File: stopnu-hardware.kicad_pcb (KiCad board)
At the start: 4 copper layers, 94 x 131 mm, 66 parts, among them CN1 SM04B-SRSS-TB (LF)(SN), CN2 OQ0232510000G, CN3 OQ0232510000G, CN4 OQ0232510000G, CN5 OQ0232510000G, CN6 OQ0432510000G, J1 Conn_02x15_Odd_Even, U1 WIFI_KIT_32__V3_, U19 SY6280AAC, U2 74HCT1G125GW-Q100H, U3 LD1117V33, U4 74HCT1G125GW-Q100H, U5 LTV-817S, U6 LTV-817S, U7 LTV-817S

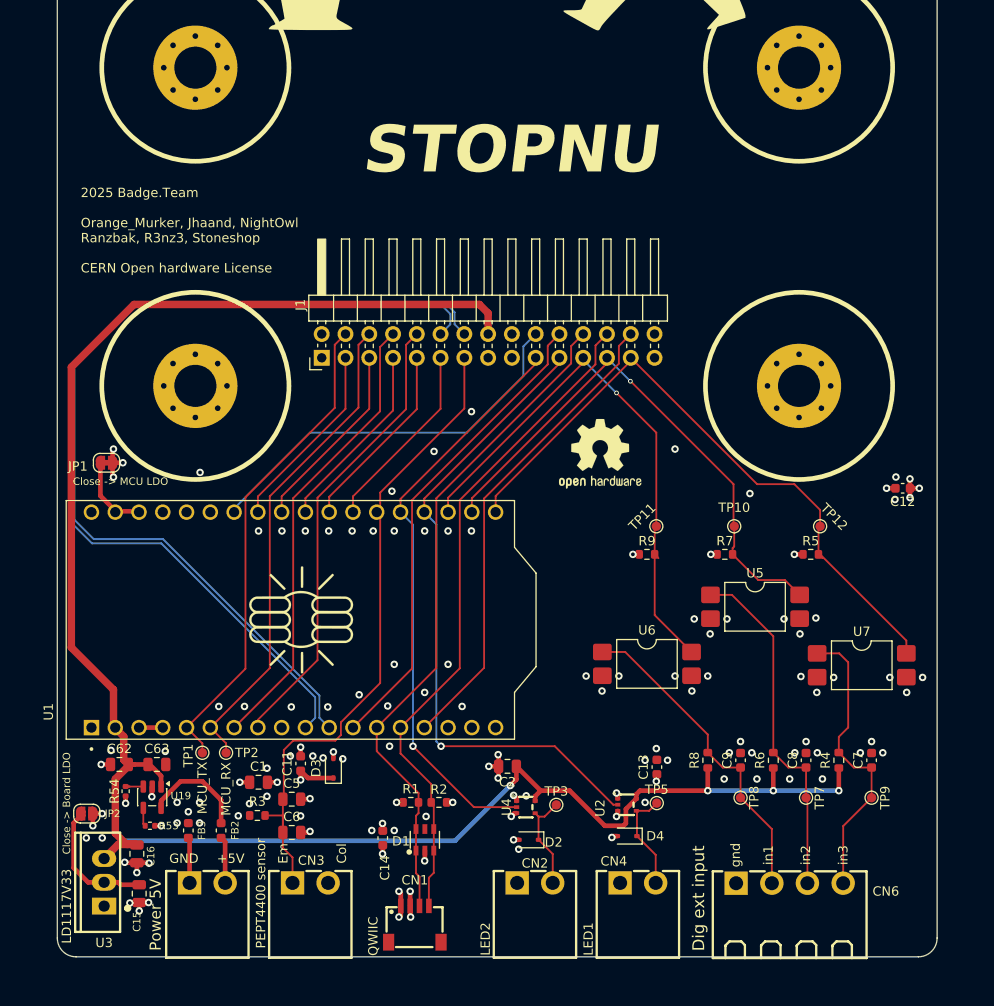
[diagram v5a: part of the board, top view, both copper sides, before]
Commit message: Labeled expansion port, fixed en pin U19 (high)
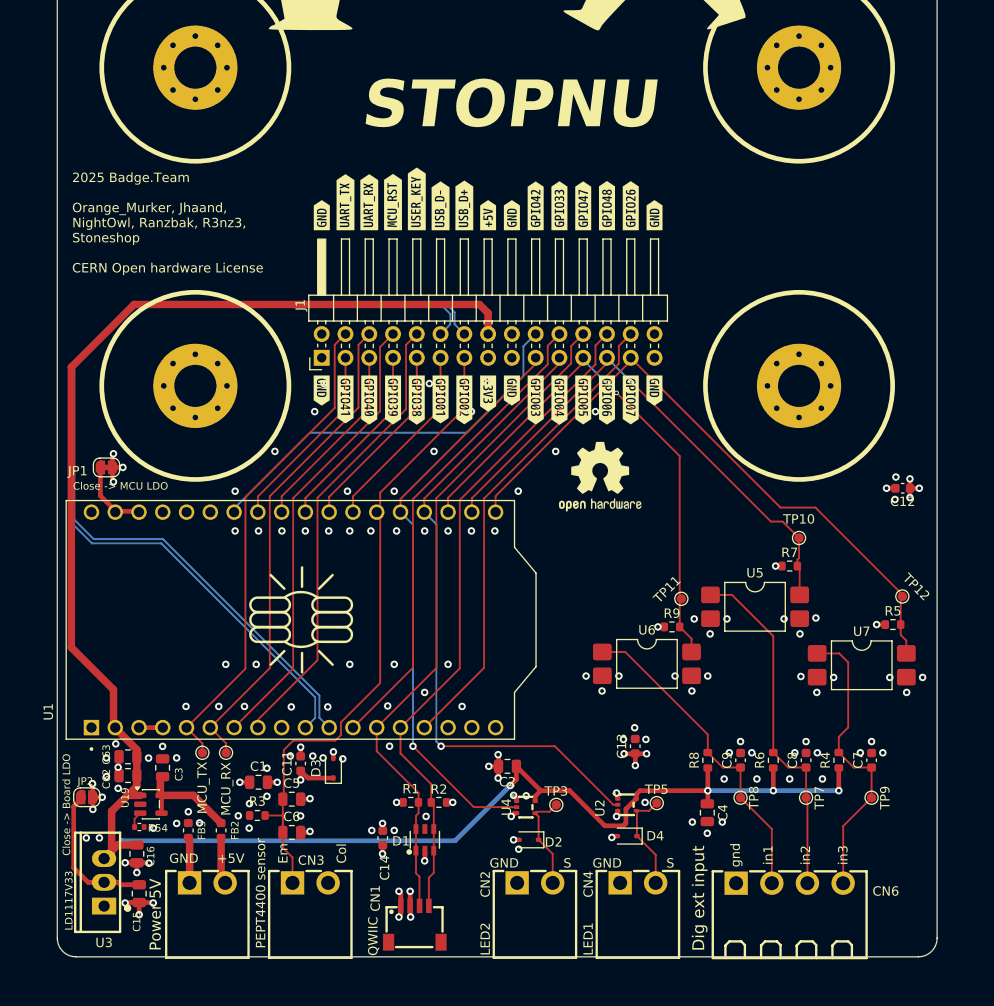
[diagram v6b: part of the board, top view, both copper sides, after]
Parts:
- removed R53: 10k, Resistor_SMD:R_0402_1005Metric
- added C3: 10u, Capacitor_SMD:C_0805_2012Metric, F.Cu at (-35.8, 57.8)
- added C4: 10u, Capacitor_SMD:C_0805_2012Metric, F.Cu at (22.4, 62.6)
- added kibuzzard-6946CCA1: G***, kibuzzard-6946CCA1, F.Cu at (16.8, 17.5)
- added kibuzzard-6946CCA1: G***, kibuzzard-6946CCA1, F.Cu at (-18.8, 17.5)
- added kibuzzard-6946CCA1: G***, kibuzzard-6946CCA1, F.Cu at (16.8, -1.24)
- added kibuzzard-6946CCA1: G***, kibuzzard-6946CCA1, F.Cu at (1.57, 17.5)
- added kibuzzard-6946CCA1: G***, kibuzzard-6946CCA1, F.Cu at (1.57, -1.24)
- added kibuzzard-6946CCA1: G***, kibuzzard-6946CCA1, F.Cu at (-18.7, -1.24)
- added kibuzzard-6946CD63: G***, kibuzzard-6946CD63, F.Cu at (14.3, 18.5)
- added kibuzzard-6946CDDB: G***, kibuzzard-6946CDDB, F.Cu at (-0.97, 17.8)
- added kibuzzard-6946CE20: G***, kibuzzard-6946CE20, F.Cu at (-8.59, 18.5)
- added kibuzzard-6946CE2E: G***, kibuzzard-6946CE2E, F.Cu at (-11.1, 18.5)
- added kibuzzard-6946CE3C: G***, kibuzzard-6946CE3C, F.Cu at (-13.7, 18.5)
- added kibuzzard-6946CE4B: G***, kibuzzard-6946CE4B, F.Cu at (-16.2, 18.4)
- added kibuzzard-6946CE82: G***, kibuzzard-6946CE82, F.Cu at (11.7, 18.5)
- added kibuzzard-6946CE89: G***, kibuzzard-6946CE89, F.Cu at (9.19, 18.5)
- added kibuzzard-6946CE92: G***, kibuzzard-6946CE92, F.Cu at (6.65, 18.5)
- added kibuzzard-6946CE98: G***, kibuzzard-6946CE98, F.Cu at (4.11, 18.5)
- added kibuzzard-6946CEA1: G***, kibuzzard-6946CEA1, F.Cu at (-3.51, 18.5)
- added kibuzzard-6946CEAD: G***, kibuzzard-6946CEAD, F.Cu at (-6.05, 18.4)
- added kibuzzard-6946CEFA: G***, kibuzzard-6946CEFA, F.Cu at (14.3, -2.25)
- added kibuzzard-6946CF08: G***, kibuzzard-6946CF08, F.Cu at (11.7, -2.26)
- added kibuzzard-6946CF12: G***, kibuzzard-6946CF12, F.Cu at (9.19, -2.24)
- added kibuzzard-6946CF20: G***, kibuzzard-6946CF20, F.Cu at (6.65, -2.25)
- added kibuzzard-6946CF2B: G***, kibuzzard-6946CF2B, F.Cu at (4.11, -2.24)
- added kibuzzard-6946CF52: G***, kibuzzard-6946CF52, F.Cu at (-0.97, -1.24)
- added kibuzzard-6946CF67: G***, kibuzzard-6946CF67, F.Cu at (-6.05, -2.24)
- added kibuzzard-6946CF7C: G***, kibuzzard-6946CF7C, F.Cu at (-3.51, -2.29)
- added kibuzzard-6946CF89: G***, kibuzzard-6946CF89, F.Cu at (-8.59, -2.98)
- added kibuzzard-6946CF95: G***, kibuzzard-6946CF95, F.Cu at (-11.1, -2.64)
- added kibuzzard-6946CFA1: G***, kibuzzard-6946CFA1, F.Cu at (-13.7, -2.63)
- added kibuzzard-6946CFA8: G***, kibuzzard-6946CFA8, F.Cu at (-16.2, -2.63)
- R3: value 10k -> 2.7k
- moved R5 11.6 mm to (42.3, 42.5)
- moved TP12 11.6 mm to (43.3, 39.5)
- moved R9 8.20 mm to (18.7, 42.8)
- moved TP11 8.20 mm to (19.7, 39.8)
- moved R7 7.04 mm to (31.2, 36.2)
- moved TP10 7.04 mm to (32.2, 33.2)
- moved R54 4.09 mm to (-38.2, 64.1), turned to 0 degrees
- moved C13 3.21 mm to (14.8, 55.5)
- moved C63 3.19 mm to (-39.5, 56.6), turned to 180 degrees
- moved N2 2.45 mm to (11.0, 26.7)
- moved JP2 1.75 mm to (-43.9, 61.0)
- moved C62 1.49 mm to (-39.4, 58.6)
- moved U19 0.76 mm to (-37.0, 61.7), turned to 0 degrees
- moved JP1 0.50 mm to (-41.7, 25.7)
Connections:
- U19 pad 4: Net-(U19-ON) -> Net-(U19-IN)
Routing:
- net +3V3: track 23.4 -> 27.8 mm, vias 19 -> 22
- net GND: track 28.3 -> 26.1 mm, vias 116 -> 133
- net Net-(U19-ON): track 2.00 -> 0.00 mm
- net /GPIO06: track 58.1 -> 56.3 mm
- net Net-(JP2-A): track 14.0 -> 15.7 mm
- net /GPIO07: track 69.2 -> 67.8 mm
- net /GPIO05: track 59.0 -> 57.6 mm
- net +5V: track 211.7 -> 211.0 mm
- net /power 5V in/+5V_EXT: track 4.99 -> 4.38 mm
- net Net-(U19-SET): track 2.29 -> 1.73 mm
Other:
- board text added: "2025 Badge.Team Orange_Murker, Jhaand, NightOwl, Ranzbak, R3nz3, Stoneshop CERN Open hardware License"
- board text added: "C_Small"
- board text removed: "2025 Badge.Team Orange_Murker, Jhaand, NightOwl Ranzbak, R3nz3, Stoneshop CERN Open hardware License"

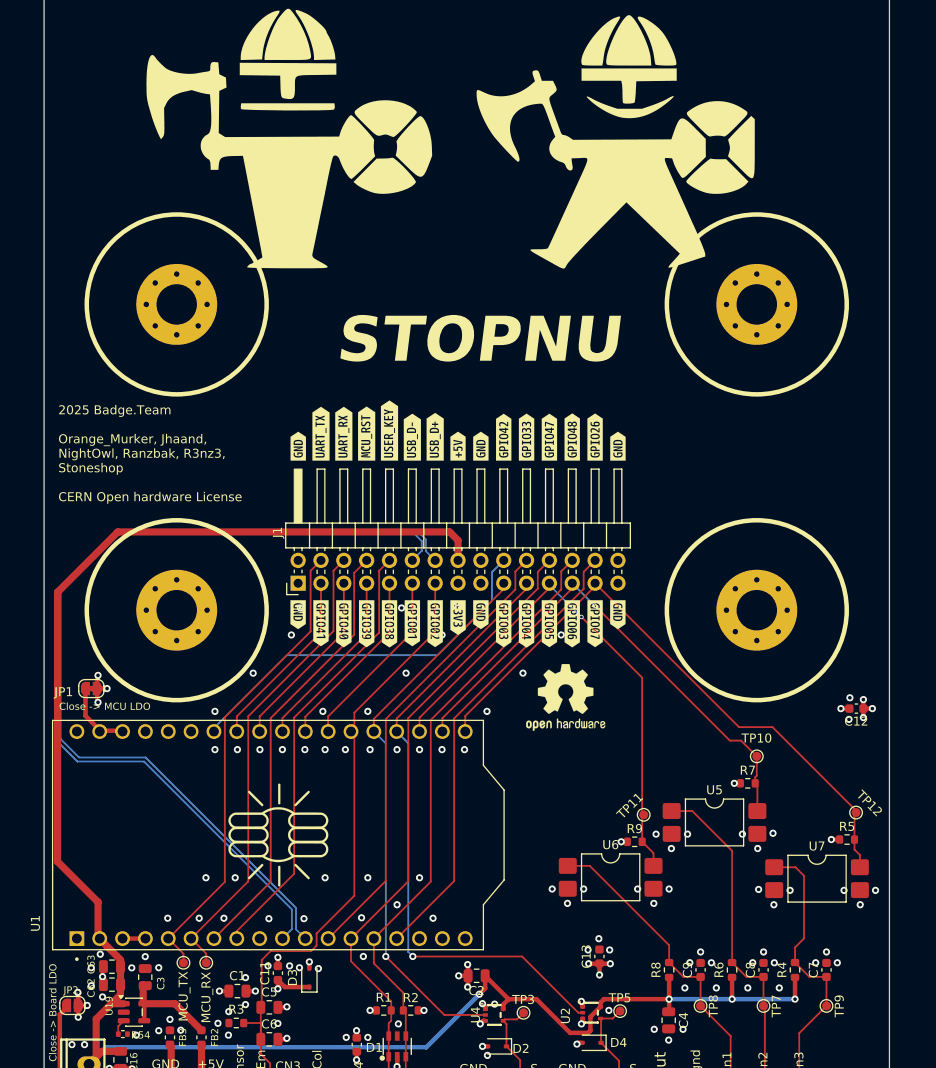
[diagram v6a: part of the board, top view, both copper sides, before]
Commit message: Fixed some pinout issues.
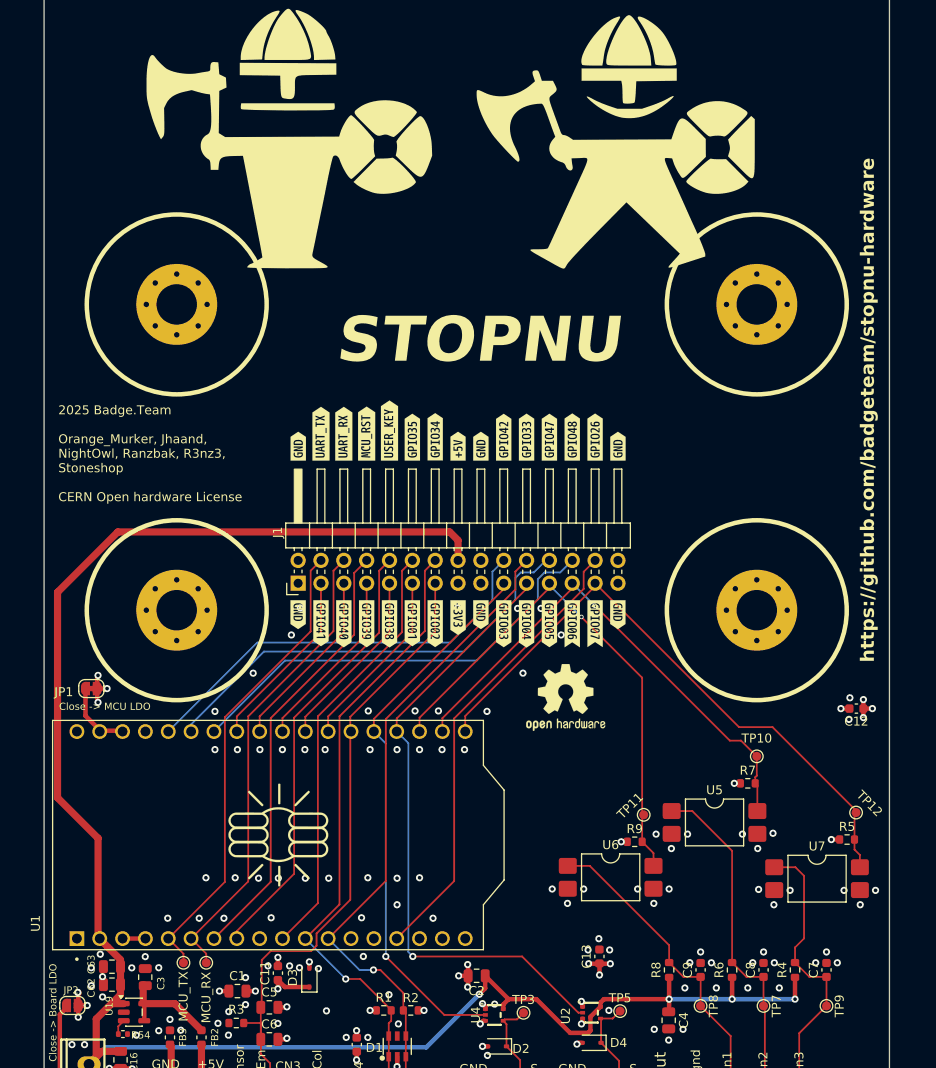
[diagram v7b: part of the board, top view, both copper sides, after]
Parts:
- removed kibuzzard-6946CD63: G***, kibuzzard-6946CD63
- removed kibuzzard-6946CE82: G***, kibuzzard-6946CE82
- removed kibuzzard-6946CF67: G***, kibuzzard-6946CF67
- removed kibuzzard-6946CF7C: G***, kibuzzard-6946CF7C
- added kibuzzard-69470A2F: G***, kibuzzard-69470A2F, F.Cu at (11.7, 18.5)
- added kibuzzard-69470A3B: G***, kibuzzard-69470A3B, F.Cu at (14.3, 18.5)
- added kibuzzard-69470A66: G***, kibuzzard-69470A66, F.Cu at (-6.05, -2.24)
- added kibuzzard-69470A71: G***, kibuzzard-69470A71, F.Cu at (-3.51, -2.29)
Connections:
- CN1 pad 3: /GPIO47 -> /GPIO34
- CN1 pad 4: /GPIO48 -> /GPIO33
- D1 pad 1: /GPIO47 -> /GPIO34
- D1 pad 3: /GPIO48 -> /GPIO33
- D1 pad 4: /GPIO48 -> /GPIO33
- D1 pad 6: /GPIO47 -> /GPIO34
- J1 pad 12: /USB_D- -> /GPIO35
- J1 pad 14: /USB_D+ -> /GPIO34
- J1 pad 20: /GPIO42 -> /GPIO45
- J1 pad 24: /GPIO47 -> /GPIO46
- J1 pad 26: /GPIO48 -> /GPIO42
- R1 pad 2: /GPIO47 -> /GPIO34
- R2 pad 2: /GPIO48 -> /GPIO33
- U1 pad J2_10: /USB_D+ -> /GPIO35
- U1 pad J2_11: /USB_D- -> /GPIO34
- U1 pad J2_13: /GPIO47 -> unconnected-(U1A-GPIO47-PadJ2_13)
- U1 pad J2_14: /GPIO48 -> unconnected-(U1A-GPIO48-PadJ2_14)
- U1 pad J2_17: /HELTEC V3/MCU_VBAT_3V3 -> unconnected-(U1A-GPIO20/U1CTS/ADC2_CH9/CLK_OUT1/USB_D+-PadJ2_17)
- U1 pad J3_5: unconnected-(U1B-GPIO46-PadJ3_5) -> /GPIO45
- U1 pad J3_6: unconnected-(U1B-GPIO45-PadJ3_6) -> /GPIO46
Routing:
- net /USB_D+: track 101.4 -> 0.00 mm
- net /USB_D-: track 99.9 -> 0.00 mm
- net /GPIO47: track 72.4 -> 0.00 mm
- net /GPIO34: track 0.00 -> 72.2 mm, vias 0 -> 1
- net /GPIO48: track 71.5 -> 0.00 mm
- net /GPIO46: track 0.00 -> 49.6 mm
- net /GPIO35: track 0.00 -> 48.0 mm
- net /GPIO45: track 0.00 -> 47.0 mm
- net /GPIO33: track 51.2 -> 75.0 mm, vias 0 -> 1
- net /GPIO42: track 41.8 -> 49.0 mm
- net GND: vias 133 -> 137
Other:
- board text added: "https://github.com/badgeteam/stopnu-hardware"
